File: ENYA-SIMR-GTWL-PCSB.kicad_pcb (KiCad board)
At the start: 4 copper layers, 30.5 x 110.5 mm, 25 parts, among them J1 PICO_BLADE_1x14_MALE_RA_SMD, J2 PICO_BLADE_1x14_MALE_RA_SMD, SW1 SKSTAJE010, SW2 SKSTAJE010, SW3 SKSTAJE010, SW4 SKSTAJE010, SW5 JS5208, SW6 JS5208, SW7 SKSTAJE010, SW8 SKSTAJE010

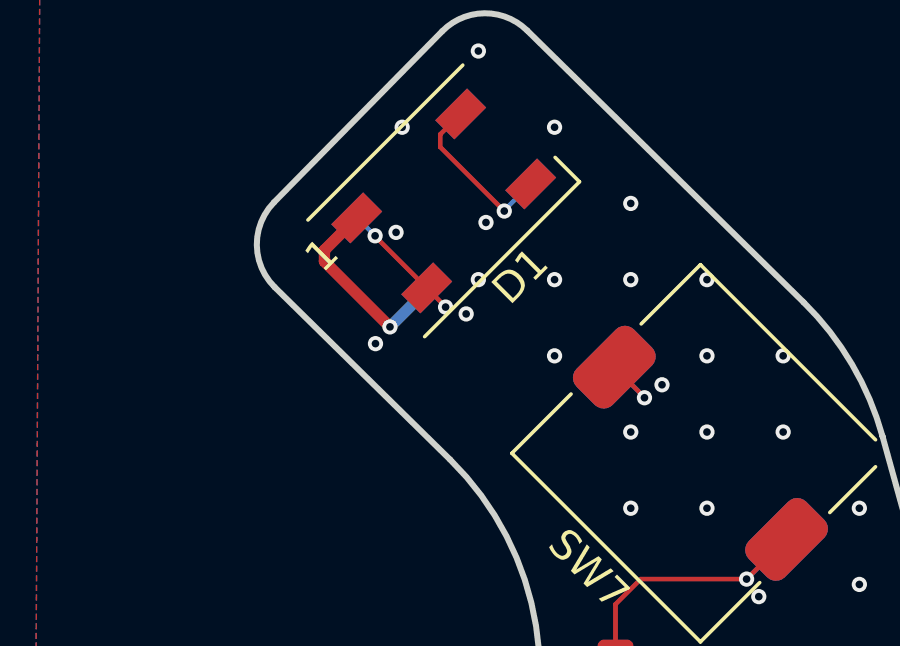
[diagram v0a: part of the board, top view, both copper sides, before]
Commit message: adding LED decoupling cap
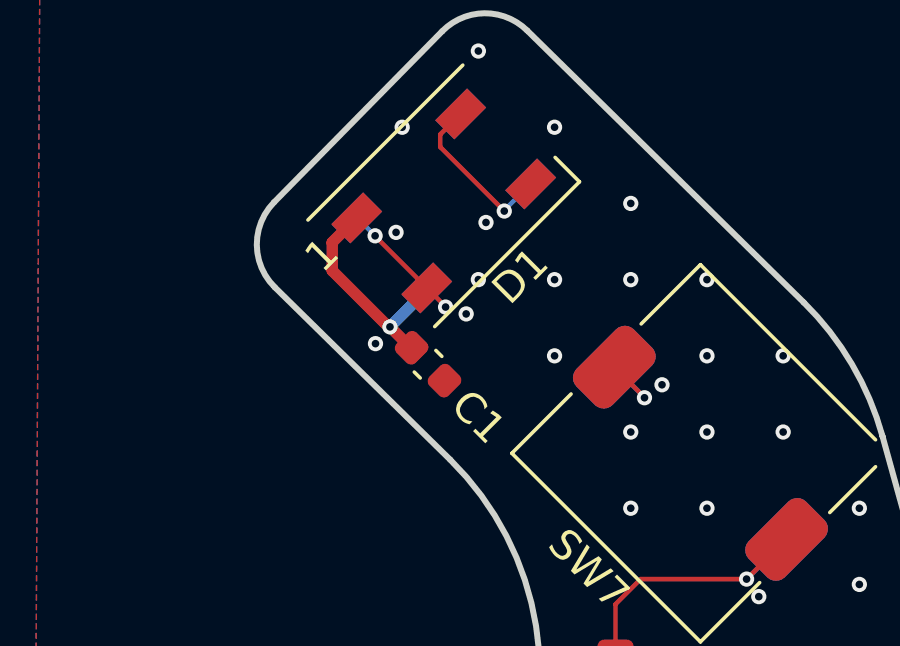
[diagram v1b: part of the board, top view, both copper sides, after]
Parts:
- added C1: 100nF_CER_0603_50V, Capacitor_SMD:C_0603_1608Metric, F.Cu at (200.3, 85.4)
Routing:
- net +5V: track 111.8 -> 112.6 mm
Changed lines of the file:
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@@
     (fp_line (start -3.65 -2.75) (end 3.65 -2.75)
       (stroke (width 0.12) (type solid)) (layer "F.SilkS"))
-    (fp_line (start -3.65 2.75) (end 3.65 2.75)
+    (fp_line (start -3.175 2.75) (end 3.65 2.75)
       (stroke (width 0.12) (type solid)) (layer "F.SilkS"))
     (fp_line (start 3.65 2.75) (end 3.65 1.6)
@@
     )
   )
+  (footprint "Capacitor_SMD:C_0603_1608Metric" (layer "F.Cu")
+    (at 200.2536 85.3694 -45)
+    (descr "Capacitor SMD 0603 (1608 Metric), square (rectangular) end terminal, IPC_7351 nominal, (Body size source: IPC-SM-782 page 76, https://www.pcb-3d.com/wordpress/wp-content/uploads/ipc-sm-782a_amendment_1_and_2.pdf), generated with kicad-footprint-generator")
+    (tags "capacitor")
+    (property "Capacitance" "100nF")
+    (property "Digi-Key Part Number" "478-7905-1-ND")
+    (property "Manufacturer" "AVX Corporation")
+    (property "Manufacturer Part Number" "06033D104MAT2A")
+    (property "Sheetfile" "ENYA-SIMR-GTWL-PCSB.kicad_sch")
+    (property "Sheetname" "")
+    (property "Voltage Rating" "50V")
+    (property "ki_description" "CAP CER 0.1UF 25V X5R 0603")
+    (property "ki_keywords" "cap capacitor")
+    (attr smd)
+    (fp_text reference "C1" (at 2.424669 0.053882 135) (layer "F.SilkS")
+        (effects (font (size 1 1) (thickness 0.15)))
+    )
+    (fp_text value "100nF_CER_0603_50V" (at 0 1.43 135) (layer "F.Fab") hide
+        (effects (font (size 1 1) (thickness 0.15)))
+    )
+    (fp_text user "${REFERENCE}" (at 0 0 135) (layer "F.Fab") hide
+        (effects (font (size 0.4 0.4) (thickness 0.06)))
+    )
+    (fp_line (start -0.14058 -0.51) (end 0.14058 -0.51)
+      (stroke (width 0.12) (type solid)) (layer "F.SilkS"))
+    (fp_line (start -0.14058 0.51) (end 0.14058 0.51)
+      (stroke (width 0.12) (type solid)) (layer "F.SilkS"))
+    (fp_line (start -1.48 -0.73) (end 1.48 -0.73)
+      (stroke (width 0.05) (type solid)) (layer "F.CrtYd"))
+    (fp_line (start -1.48 0.73) (end -1.48 -0.73)
+      (stroke (width 0.05) (type solid)) (layer "F.CrtYd"))
+    (fp_line (start 1.48 -0.73) (end 1.48 0.73)
+      (stroke (width 0.05) (type solid)) (layer "F.CrtYd"))
+    (fp_line (start 1.48 0.73) (end -1.48 0.73)
+      (stroke (width 0.05) (type solid)) (layer "F.CrtYd"))
+    (fp_line (start -0.8 -0.4) (end 0.8 -0.4)
+      (stroke (width 0.1) (type solid)) (layer "F.Fab"))
+    (fp_line (start -0.8 0.4) (end -0.8 -0.4)
+      (stroke (width 0.1) (type solid)) (layer "F.Fab"))
+    (fp_line (start 0.8 -0.4) (end 0.8 0.4)
+      (stroke (width 0.1) (type solid)) (layer "F.Fab"))
+    (fp_line (start 0.8 0.4) (end -0.8 0.4)
+      (stroke (width 0.1) (type solid)) (layer "F.Fab"))
+    (pad "1" smd roundrect (at -0.775 0 315) (size 0.9 0.95) (layers "F.Cu" "F.Paste" "F.Mask") (roundrect_rratio 0.25)
+      (net 1 "+5V") (pintype "passive"))
+    (pad "2" smd roundrect (at 0.775 0 315) (size 0.9 0.95) (layers "F.Cu" "F.Paste" "F.Mask") (roundrect_rratio 0.25)
+      (net 3 "GND") (pintype "passive"))
+    (model "${KICAD6_3DMODEL_DIR}/Capacitor_SMD.3dshapes/C_0603_1608Metric.wrl"
+      (offset (xyz 0 0 0))
+      (scale (xyz 1 1 1))
+      (rotate (xyz 0 0 0))
+    )
+  )
   (footprint "ENYA_Connector_PicoBlade:PICO_BLADE_53261_1x14_SMD_RA_1.25MM" locked (layer "F.Cu")
     (at 203.17132 169.753376 -100)
@@
     (effects (font (size 0.889 0.889) (thickness 0.15)) (justify bottom))
   )
-  (segment (start 196.7992 81.9404) (end 196.7992 81.568031) (width 0.381) (layer "F.Cu") (net 1))
+  (segment (start 197.057016 81.310215) (end 197.876125 80.491106) (width 0.381) (layer "F.Cu") (net 1))
+  (segment (start 197.057016 82.249016) (end 197.057016 81.310215) (width 0.381) (layer "F.Cu") (net 1))
   (segment (start 203.4286 178.1302) (end 204.488052 178.1302) (width 0.381) (layer "F.Cu") (net 1))
-  (segment (start 196.7992 81.568031) (end 197.876125 80.491106) (width 0.381) (layer "F.Cu") (net 1))
+  (segment (start 199.680192 84.821392) (end 199.705592 84.821392) (width 0.381) (layer "F.Cu") (net 1))
   (segment (start 204.488052 178.1302) (end 204.616371 178.258519) (width 0.381) (layer "F.Cu") (net 1))
-  (segment (start 198.9836 84.1248) (end 196.7992 81.9404) (width 0.381) (layer "F.Cu") (net 1))
+  (segment (start 198.9836 84.1248) (end 199.680192 84.821392) (width 0.381) (layer "F.Cu") (net 1))
+  (segment (start 198.9328 84.1248) (end 197.057016 82.249016) (width 0.381) (layer "F.Cu") (net 1))
+  (segment (start 198.9836 84.1248) (end 198.9328 84.1248) (width 0.381) (layer "F.Cu") (net 1))
   (segment (start 203.4286 178.1302) (end 203.1238 177.8254) (width 0.381) (layer "F.Cu") (net 1))
   (via (at 198.9836 84.1248) (size 0.508) (drill 0.254) (layers "F.Cu" "B.Cu") (net 1))
@@
     (connect_pads (clearance 0.2032))
     (min_thickness 0.254) (filled_areas_thickness no)
-    (fill yes (thermal_gap 0.508) (thermal_bridge_width 0.508) (smoothing fillet) (radius 0.635))
+    (fill yes (thermal_gap 0.254) (thermal_bridge_width 0.508) (smoothing fillet) (radius 0.635))
     (polygon
       (pts

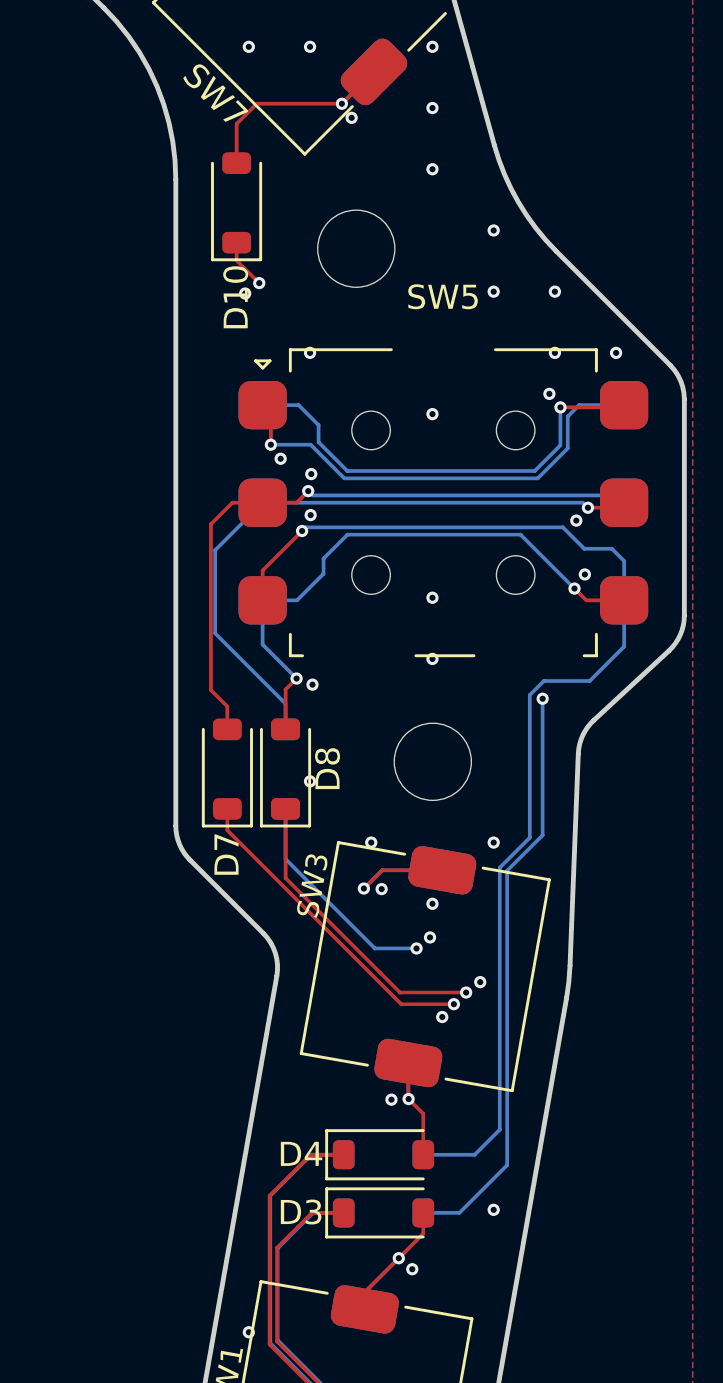
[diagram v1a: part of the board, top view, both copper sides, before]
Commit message: correction button matrix diode polarity
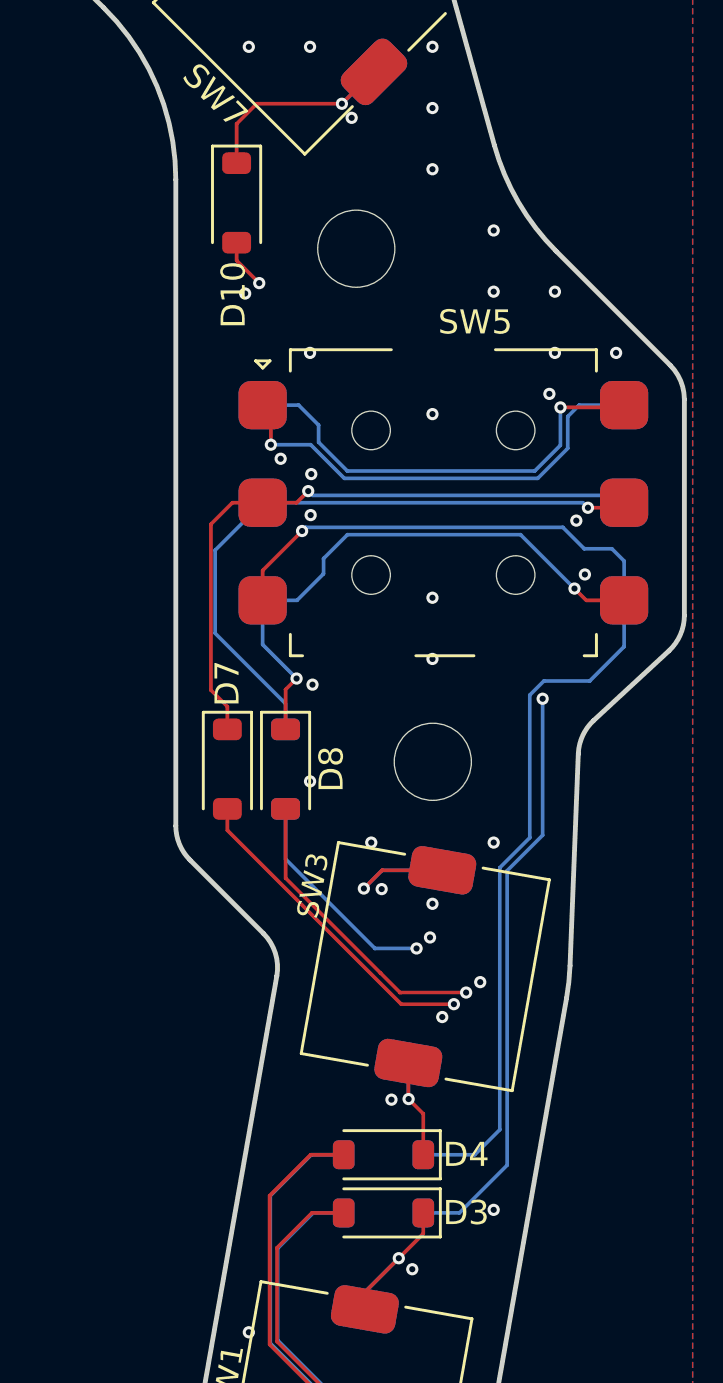
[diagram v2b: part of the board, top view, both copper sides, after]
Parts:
- turned D10 to -90 degrees
- turned D3 to 180 degrees
- turned D4 to 180 degrees
- turned D5 to 180 degrees
- turned D6 to 180 degrees
- turned D7 to -90 degrees
- turned D8 to -90 degrees
- turned D9 to -90 degrees
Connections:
- D10 pad 1: /BTN_ROW7 -> Net-(D10-K)
- D10 pad 2: Net-(D10-A) -> /BTN_ROW7
- D3 pad 1: /BTN_ROW0 -> Net-(D3-K)
- D3 pad 2: Net-(D3-A) -> /BTN_ROW0
- D4 pad 1: /BTN_ROW1 -> Net-(D4-K)
- D4 pad 2: Net-(D4-A) -> /BTN_ROW1
- D5 pad 1: /BTN_ROW2 -> Net-(D5-K)
- D5 pad 2: Net-(D5-A) -> /BTN_ROW2
- D6 pad 1: /BTN_ROW3 -> Net-(D6-K)
- D6 pad 2: Net-(D6-A) -> /BTN_ROW3
- D7 pad 1: /BTN_ROW4 -> Net-(D7-K)
- D7 pad 2: Net-(D7-A) -> /BTN_ROW4
- D8 pad 1: /BTN_ROW5 -> Net-(D8-K)
- D8 pad 2: Net-(D8-A) -> /BTN_ROW5
- D9 pad 1: /BTN_ROW6 -> Net-(D9-K)
- D9 pad 2: Net-(D9-A) -> /BTN_ROW6
- SW1 pad 2: Net-(D3-A) -> Net-(D3-K)
- SW2 pad 2: Net-(D3-A) -> Net-(D3-K)
- SW3 pad 2: Net-(D4-A) -> Net-(D4-K)
- SW4 pad 2: Net-(D4-A) -> Net-(D4-K)
- SW5 pad 2: Net-(D7-A) -> Net-(D7-K)
- SW5 pad 3: Net-(D5-A) -> Net-(D5-K)
- SW5 pad 4: Net-(D6-A) -> Net-(D6-K)
- SW5 pad 5: Net-(D9-A) -> Net-(D9-K)
- SW5 pad 6: Net-(D8-A) -> Net-(D8-K)
- SW6 pad 2: Net-(D7-A) -> Net-(D7-K)
- SW6 pad 3: Net-(D5-A) -> Net-(D5-K)
- SW6 pad 4: Net-(D6-A) -> Net-(D6-K)
- SW6 pad 5: Net-(D9-A) -> Net-(D9-K)
- SW6 pad 6: Net-(D8-A) -> Net-(D8-K)
- SW7 pad 2: Net-(D10-A) -> Net-(D10-K)
- SW8 pad 2: Net-(D10-A) -> Net-(D10-K)
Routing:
- net Net-(D6-K): track 0.00 -> 58.1 mm, vias 0 -> 2
- net Net-(D6-A): track 58.1 -> 0.00 mm, vias 2 -> 0
- net Net-(D5-K): track 0.00 -> 48.0 mm, vias 0 -> 1
- net Net-(D5-A): track 48.0 -> 0.00 mm, vias 1 -> 0
- net Net-(D7-K): track 0.00 -> 26.7 mm, vias 0 -> 1
- net Net-(D7-A): track 26.7 -> 0.00 mm, vias 1 -> 0
- net Net-(D9-K): track 0.00 -> 26.6 mm, vias 0 -> 1
- net Net-(D9-A): track 26.6 -> 0.00 mm, vias 1 -> 0
- net Net-(D8-K): track 0.00 -> 23.8 mm, vias 0 -> 2
- net Net-(D8-A): track 23.8 -> 0.00 mm, vias 2 -> 0
- net Net-(D10-K): track 0.00 -> 10.1 mm, vias 0 -> 1
- net Net-(D10-A): track 10.1 -> 0.00 mm, vias 1 -> 0
- net Net-(D3-K): track 0.00 -> 7.71 mm, vias 0 -> 1
- net Net-(D3-A): track 7.71 -> 0.00 mm, vias 1 -> 0
- net Net-(D4-K): track 0.00 -> 5.57 mm, vias 0 -> 1
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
